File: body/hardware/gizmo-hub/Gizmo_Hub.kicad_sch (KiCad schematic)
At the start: 19 parts, among them J1 DISPLAY, J10 FUTURE, J2 SPEAKER 3885, J3 BUTTONS, J4 PTT, J5 HAPTIC, J6 PWR, J7 UTIL, J8 5V AUX A, J9 5V AUX B, U1 XIAO ESP32S3 Sense

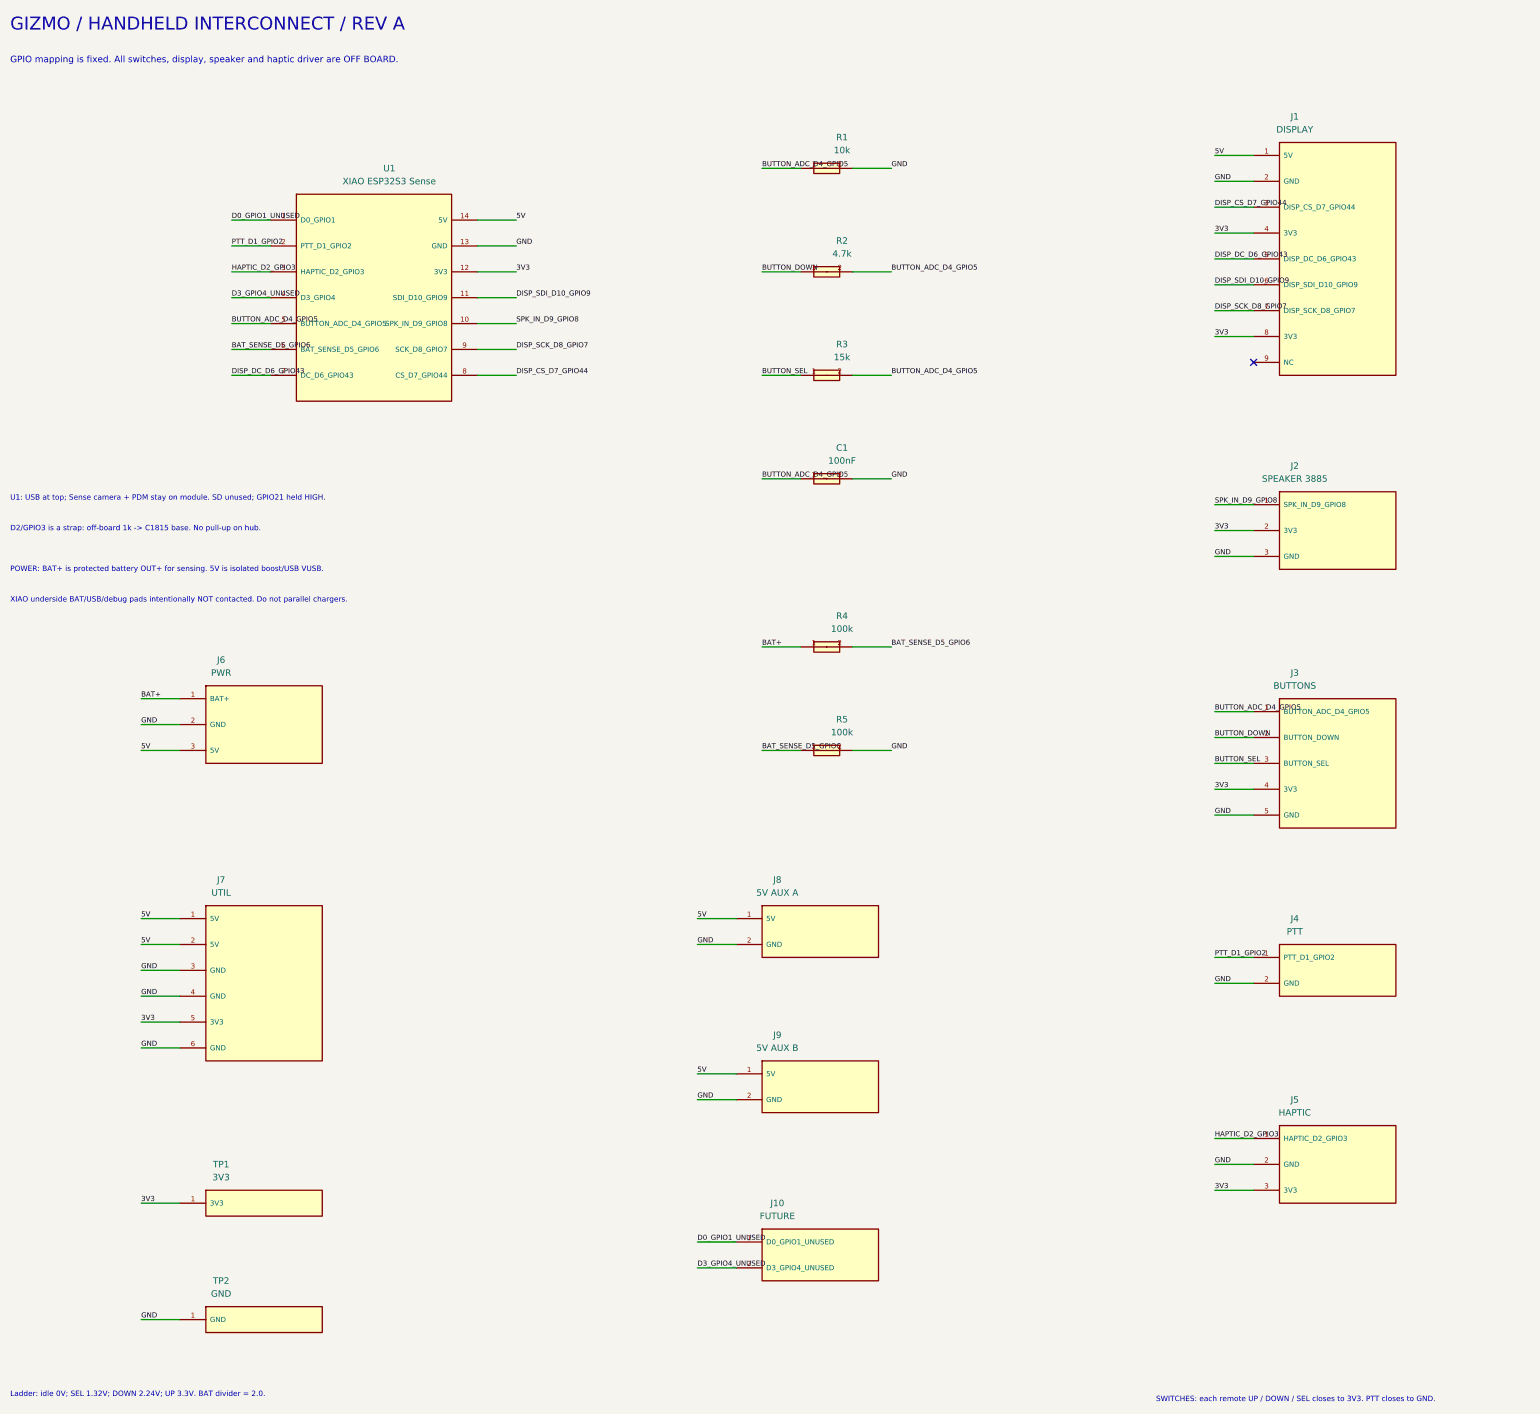
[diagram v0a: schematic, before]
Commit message: Complete Gizmo hub routing, battery clearance, and wiring documentation
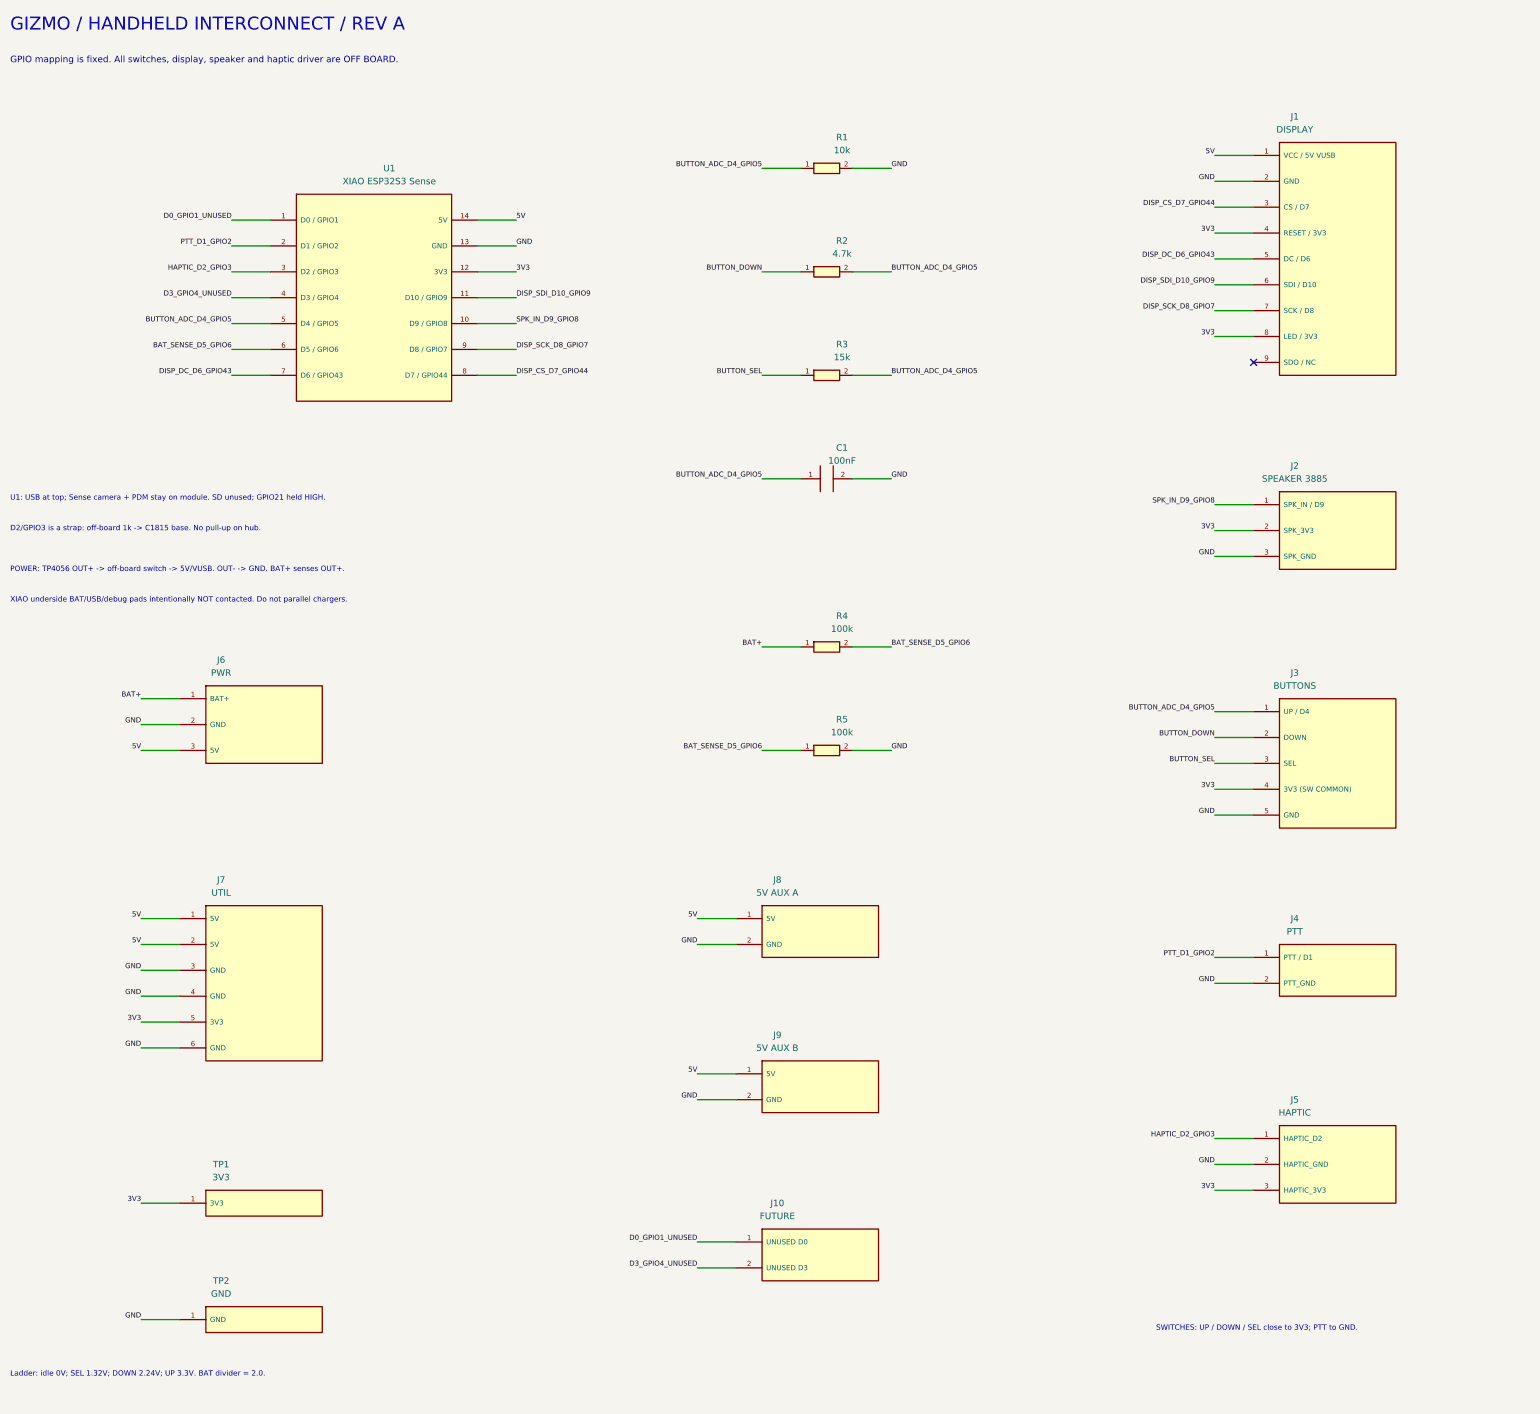
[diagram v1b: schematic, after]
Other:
- note added: "POWER: TP4056 OUT+ -> off-board switch -> 5V/VUSB. OUT- -> GND. BAT+ senses OUT+."
- note added: "SWITCHES: UP / DOWN / SEL close to 3V3; PTT to GND."
- note removed: "POWER: BAT+ is protected battery OUT+ for sensing. 5V is isolated boost/USB VUSB."
- note removed: "SWITCHES: each remote UP / DOWN / SEL closes to 3V3. PTT closes to GND."
